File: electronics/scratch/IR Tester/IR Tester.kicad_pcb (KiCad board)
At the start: 2 copper layers, 34 parts, among them J1 VS RAW, J10 IR TX AOE, J2 APA RAW, J3 XL RAW, Q3 AO3406, Q4 AO3406, Q5 AO3406, Q6 AO3406, U1 VSMB10940, U2 VSMB10940, U3 XL-3210IRC-940, U4 XL-3210IRC-940

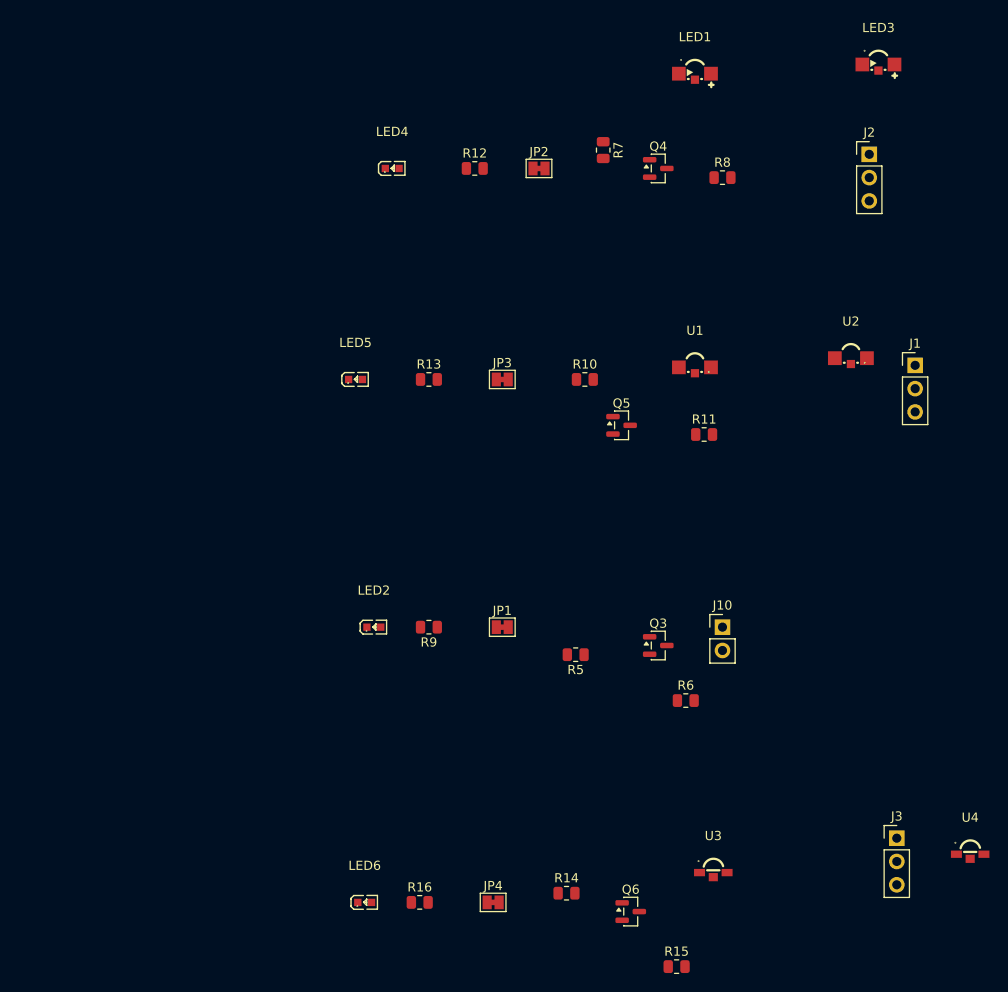
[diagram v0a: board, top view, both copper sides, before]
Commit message: IR tester board traced, parts assigned, sent to PCBWay
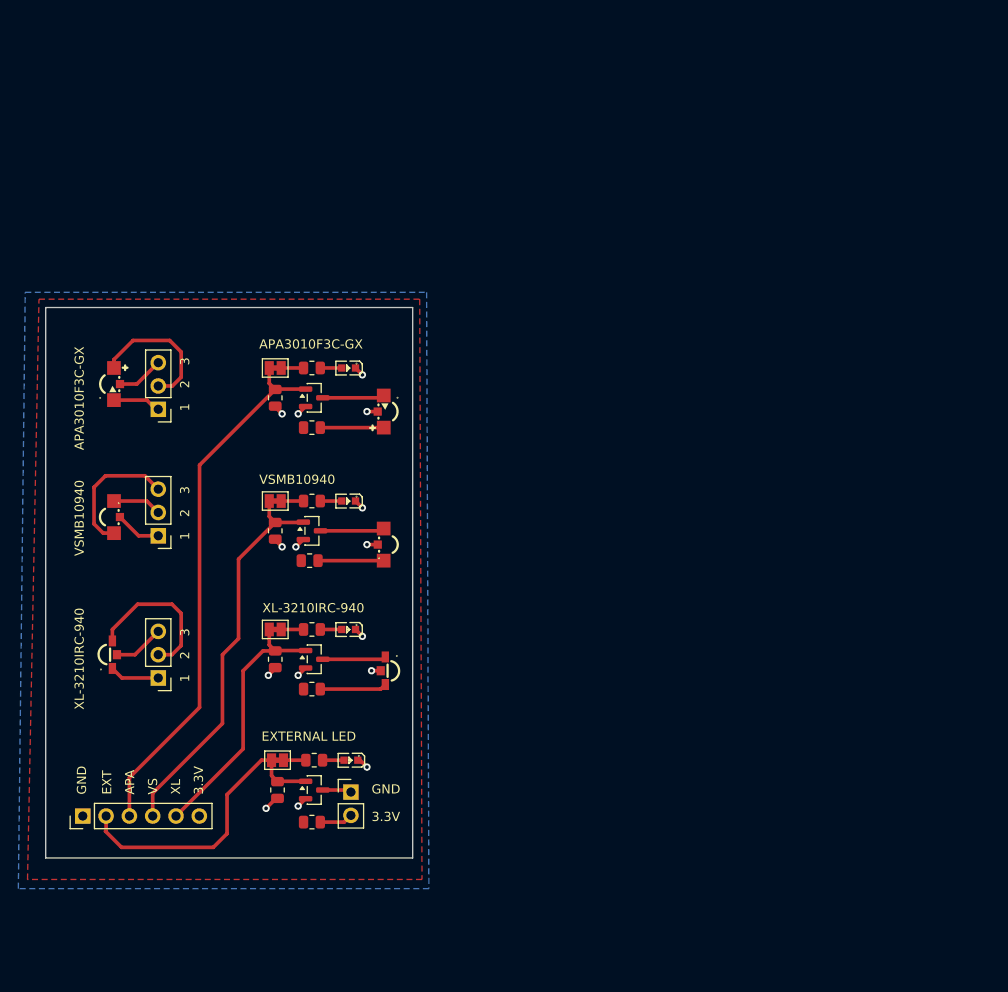
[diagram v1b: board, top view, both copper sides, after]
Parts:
- added J4: Breakout Pins, Connector_PinHeader_2.54mm:PinHeader_1x06_P2.54mm_Vertical, F.Cu at (66.3, 137.6)
- moved U4 95.8 mm to (69.8, 120.0), turned to 90 degrees
- moved LED3 89.9 mm to (70.0, 90.5), turned to 90 degrees
- moved J1 84.6 mm to (74.5, 107.0), turned to 180 degrees
- moved J3 82.4 mm to (74.5, 122.5), turned to 180 degrees
- moved J2 82.3 mm to (74.5, 93.2), turned to 180 degrees
- moved U2 81.8 mm to (70.0, 105.0), turned to 90 degrees
- moved R8 52.4 mm to (91.2, 95.2)
- moved LED1 50.1 mm to (98.8, 93.5), turned to -90 degrees
- moved R15 50.0 mm to (91.2, 123.8)
- moved R11 45.1 mm to (91.0, 109.8)
- moved Q4 45.1 mm to (91.5, 92.0)
- moved R7 44.8 mm to (87.2, 92.0)
- moved J10 44.3 mm to (95.5, 135.0)
- moved Q6 44.1 mm to (91.5, 120.5)
- moved R6 42.9 mm to (91.2, 138.2)
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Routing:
- net /APA 50: track 0.00 -> 59.0 mm
- net /VS 65: track 0.00 -> 43.2 mm
- net /IR TX: track 0.00 -> 32.6 mm
- net /XL 21: track 0.00 -> 29.2 mm
- net GND: track 0.00 -> 17.6 mm, vias 0 -> 15
- net Net-(J3-Pin_2): track 0.00 -> 16.7 mm
- net Net-(J2-Pin_2): track 0.00 -> 15.3 mm
- net Net-(J1-Pin_3): track 0.00 -> 14.7 mm
- net Net-(R15-Pad2): track 0.00 -> 7.29 mm
- net Net-(R11-Pad2): track 0.00 -> 7.16 mm
- net Net-(Q5-D): track 0.00 -> 6.99 mm
- net Net-(LED1-A): track 0.00 -> 6.92 mm
- net Net-(Q6-D): track 0.00 -> 6.92 mm
- net Net-(LED1-K): track 0.00 -> 6.75 mm
- net Net-(J3-Pin_3): track 0.00 -> 5.55 mm
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- added copper zone on F.Cu, net +3.3V
- added copper zone on B.Cu, net GND
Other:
- board outline added: 40 x 60 mm
- board text added: "1"
- board text added: "2"
- board text added: "3"
- board text added: "3.3V"
- board text added: "APA"
- board text added: "APA3010F3C-GX"
- board text added: "EXT"
- board text added: "EXTERNAL LED"
- board text added: "GND"
- board text added: "VS"
- board text added: "VSMB10940"
- board text added: "XL"
- board text added: "XL-3210IRC-940"

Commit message: IR Tester - correct VSMB10940 polarity an amp circuit
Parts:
- moved R11 10.9 mm to (99.0, 102.3), turned to -90 degrees
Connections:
- U1 pad 2: Net-(R11-Pad2) -> Net-(Q5-D)
- U1 pad 3: Net-(Q5-D) -> Net-(R11-Pad2)
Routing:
- net Net-(R11-Pad2): track 7.16 -> 3.42 mm
- net Net-(Q5-D): track 6.99 -> 8.23 mm
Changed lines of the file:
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@@
 	(footprint "Resistor_SMD:R_0805_2012Metric"
 		(layer "F.Cu")
-		(at 91 109.75)
+		(at 99 102.3 -90)
 		(descr "Resistor SMD 0805 (2012 Metric), square (rectangular) end terminal, IPC-7351 nominal, (Body size source: IPC-SM-782 page 72, https://www.pcb-3d.com/wordpress/wp-content/uploads/ipc-sm-782a_amendment_1_and_2.pdf)")
 		(tags "resistor")
 		(property "Reference" "R11"
-			(at 0 -1.65 0)
+			(at 0 -1.65 90)
 			(layer "F.SilkS")
 			(hide yes)
@@
 		)
 		(property "Value" "30"
-			(at 0 1.65 0)
+			(at 0 1.65 90)
 			(layer "F.Fab")
 			(effects
@@
 		)
 		(property "Datasheet" ""
-			(at 0 0 0)
+			(at 0 0 90)
 			(layer "F.Fab")
 			(hide yes)
@@
 		)
 		(property "Description" "Resistor"
-			(at 0 0 0)
+			(at 0 0 90)
 			(layer "F.Fab")
 			(hide yes)
@@
 		)
 		(property "KiLib_Generator" "SMD_2terminal_chip_molded"
-			(at 0 0 0)
+			(at 0 0 90)
 			(layer "F.SilkS")
 			(hide yes)
@@
 		)
 		(property "LCSC Part" "C17622"
-			(at 0 0 0)
+			(at 0 0 270)
 			(unlocked yes)
 			(layer "F.Fab")
@@
 		)
 		(property "Manufacturer" "UNI-ROYAL"
-			(at 0 0 0)
+			(at 0 0 270)
 			(unlocked yes)
 			(layer "F.Fab")
@@
 		)
 		(property "MPN" "0805W8F300JT5E"
-			(at 0 0 0)
+			(at 0 0 270)
 			(unlocked yes)
 			(layer "F.Fab")
@@
 		(duplicate_pad_numbers_are_jumpers no)
 		(fp_line
-			(start -0.227064 -0.735)
-			(end 0.227064 -0.735)
+			(start -0.227064 0.735)
+			(end 0.227064 0.735)
 			(stroke
 				(width 0.12)
@@
 		)
 		(fp_line
-			(start -0.227064 0.735)
-			(end 0.227064 0.735)
+			(start -0.227064 -0.735)
+			(end 0.227064 -0.735)
 			(stroke
 				(width 0.12)
@@
 		)
 		(fp_text user "${REFERENCE}"
-			(at 0 0 0)
+			(at 0 0 90)
 			(layer "F.Fab")
 			(effects
@@
 		)
 		(pad "1" smd roundrect
-			(at -0.9125 0)
+			(at -0.9125 0 270)
 			(size 1.025 1.4)
 			(layers "F.Cu" "F.Mask" "F.Paste")
@@
 		)
 		(pad "2" smd roundrect
-			(at 0.9125 0)
+			(at 0.9125 0 270)
 			(size 1.025 1.4)
 			(layers "F.Cu" "F.Mask" "F.Paste")
@@
 			(size 1.5 1.5)
 			(layers "F.Cu" "F.Mask" "F.Paste")
-			(net "Net-(R11-Pad2)")
+			(net "Net-(Q5-D)")
 			(pinfunction "2_2")
 			(pintype "unspecified")
@@
 			(size 1.5 1.5)
 			(layers "F.Cu" "F.Mask" "F.Paste")
-			(net "Net-(Q5-D)")
+			(net "Net-(R11-Pad2)")
 			(pinfunction "3_3")
 			(pintype "unspecified")
@@
 				(font
 					(size 1.27 1.27)
+					(thickness 0.15)
 				)
 			)
@@
 	)
 	(segment
+		(start 96.85 109.75)
+		(end 99.07 109.75)
+		(width 0.2)
+		(layer "F.Cu")
+		(net "Net-(Q5-D)")
+	)
+	(segment
 		(start 92.1875 106.5)
-		(end 98.82 106.5)
-		(width 0.4)
+		(end 93.6 106.5)
+		(width 0.2)
 		(layer "F.Cu")
 		(net "Net-(Q5-D)")
 	)
 	(segment
-		(start 98.82 106.5)
-		(end 99.07 106.25)
-		(width 0.4)
+		(start 93.6 106.5)
+		(end 96.85 109.75)
+		(width 0.2)
 		(layer "F.Cu")
 		(net "Net-(Q5-D)")
@@
 	)
 	(segment
-		(start 91.9125 109.75)
-		(end 99.07 109.75)
+		(start 99 103.2125)
+		(end 99 106.18)
+		(width 0.2)
+		(layer "F.Cu")
+		(net "Net-(R11-Pad2)")
+	)
+	(segment
+		(start 99 106.18)
+		(end 99.07 106.25)
+		(width 0.2)
+		(layer "F.Cu")
+		(net "Net-(R11-Pad2)")
+	)
+	(segment
+		(start 98.82 106.5)
+		(end 99.07 106.25)
 		(width 0.4)
 		(layer "F.Cu")
